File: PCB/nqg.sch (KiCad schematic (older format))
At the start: 76 parts, among them SW1 SW_PUSH, SW10 SW_PUSH, SW11 SW_PUSH, SW12 SW_PUSH, SW13 SW_PUSH, SW14 SW_PUSH, SW15 SW_PUSH, SW16 SW_PUSH, SW17 SW_PUSH, SW18 SW_PUSH, SW19 SW_PUSH, SW2 SW_PUSH, SW20 SW_PUSH, SW21 SW_PUSH, SW22 SW_PUSH, SW23 SW_PUSH, SW24 SW_PUSH, SW25 SW_PUSH, SW26 SW_PUSH, SW27 SW_PUSH, SW28 SW_PUSH, SW29 SW_PUSH, SW3 SW_PUSH, SW30 SW_PUSH, SW31 SW_PUSH, SW32 SW_PUSH, SW33 SW_PUSH, SW34 SW_PUSH, SW35 SW_PUSH, SW36 SW_PUSH, SW37 SW_PUSH, SW38 SW_PUSH, SW39 SW_PUSH, SW4 SW_PUSH, SW40 SW_PUSH, SW5 SW_PUSH, SW6 SW_PUSH, SW7 SW_PUSH, SW8 SW_PUSH, SW9 SW_PUSH, U1 ProMicro

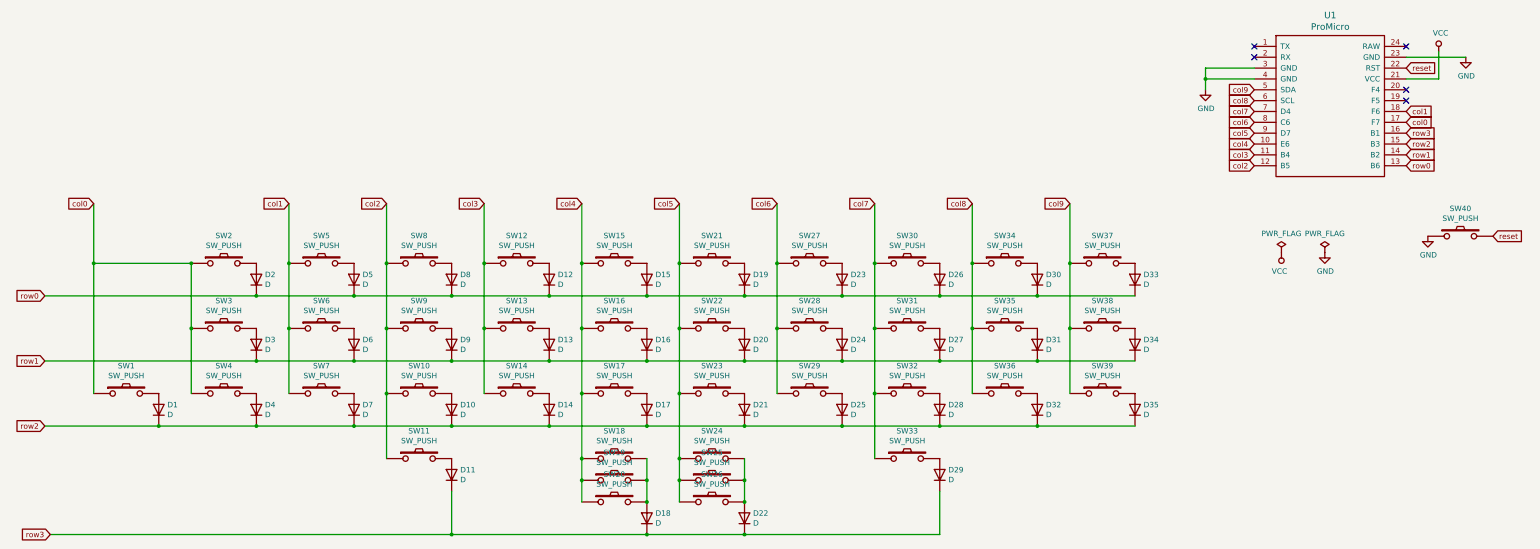
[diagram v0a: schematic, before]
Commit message: redid wiring, firmware halfway done
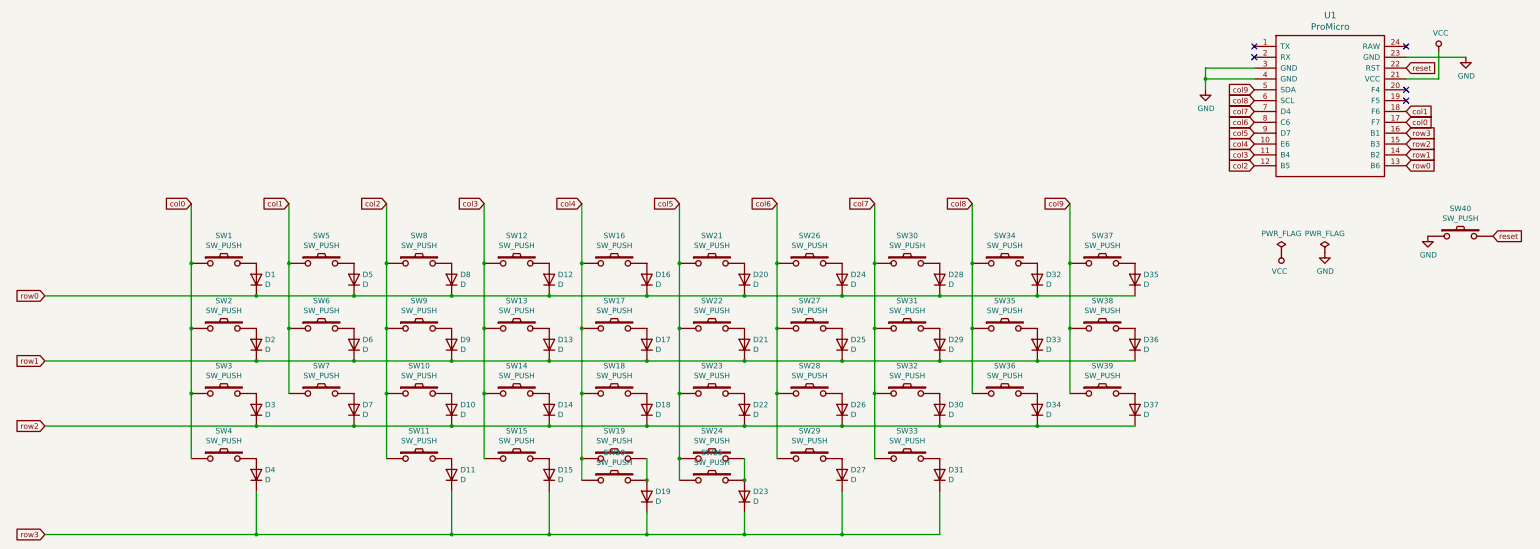
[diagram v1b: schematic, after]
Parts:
- added D15, D27: D, Diode_SMD:D_SOD-123, symbol Device:D
- renumbered D2 to D1, D15 to D16, D16 to D17, D17 to D18, D18 to D19, D3 to D2, D19 to D20, D20 to D21, D21 to D22, D22 to D23, D23 to D24, D24 to D25, D25 to D26, D26 to D28, D27 to D29, D4 to D3, D28 to D30, D29 to D31, D30 to D32, D31 to D33, D32 to D34, D33 to D35, D34 to D36, D35 to D37, D1 to D4, SW2 to SW1, SW20 to SW15, SW15 to SW16, SW16 to SW17, SW17 to SW18, SW18 to SW19, SW3 to SW2, SW19 to SW20, SW27 to SW26, SW28 to SW27, SW29 to SW28, SW26 to SW29, SW4 to SW3, SW1 to SW4
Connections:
- net col3: now also SW15.1
- net col4: no longer SW15.1
- net col5: no longer SW29.1
- net col6: now also SW29.1
- net row2: no longer D4.1 (K)
- net row3: now also D4.1 (K), D15.1 (K), D27.1 (K)
- net at D19.2 (A), SW19.2, SW20.2: no longer SW15.2
- net at D23.2 (A), SW24.2, SW25.2: no longer SW29.2
- new net: D15.2 (A), SW15.2
- new net: D27.2 (A), SW29.2
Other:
- moved on the sheet: D19, D23, D4, SW15, SW29, SW4

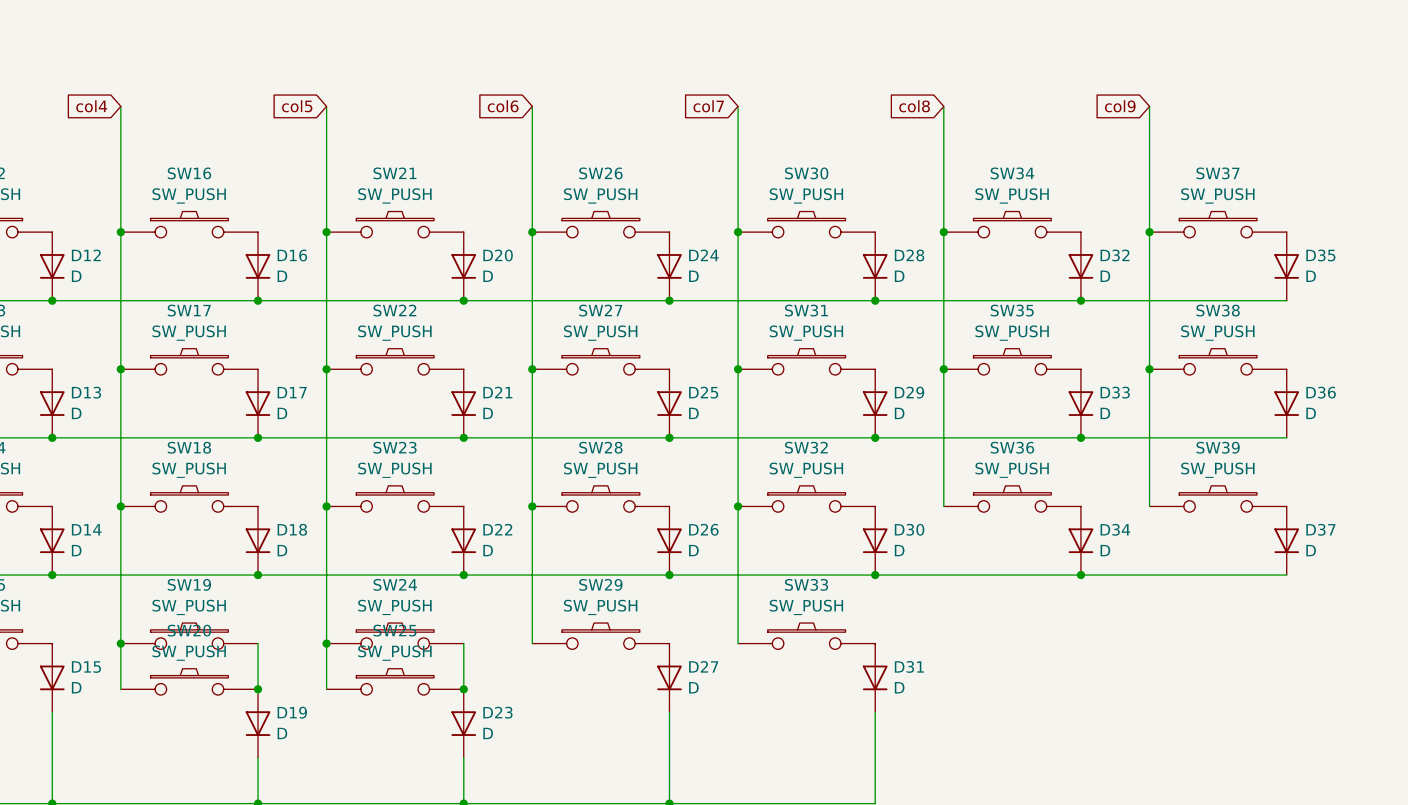
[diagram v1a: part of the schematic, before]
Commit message: now switch # matches up with diode # in SMD version as well
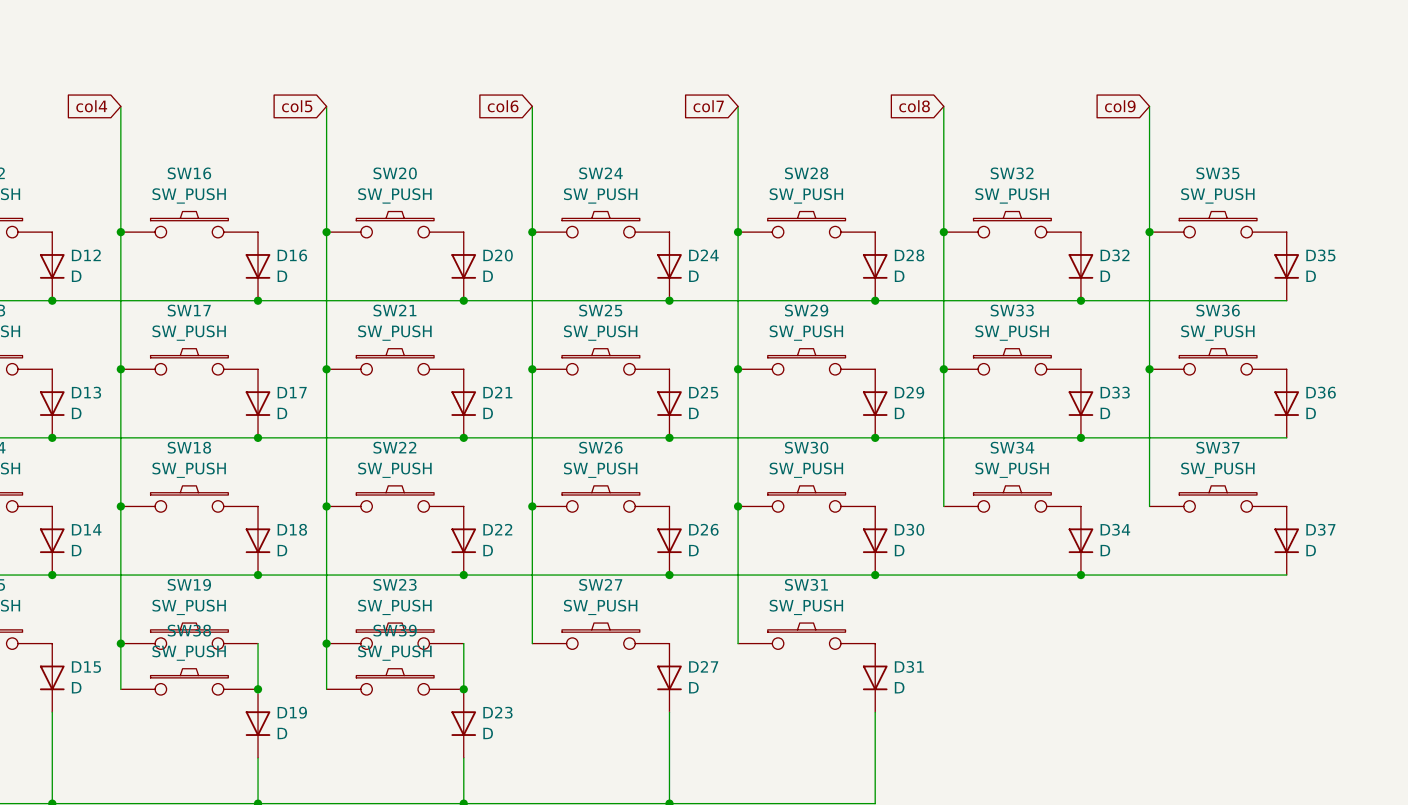
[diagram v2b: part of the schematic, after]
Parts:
- removed SW20, SW25: SW_PUSH, kbd:CherryMX_Hotswap_Back, symbol kbd:SW_PUSH
- added SW38, SW39: SW_PUSH, kbd:CherryMX_Hotswap_Back, symbol kbd:SW_PUSH
- renumbered SW21 to SW20, SW22 to SW21, SW23 to SW22, SW24 to SW23, SW26 to SW24, SW27 to SW25, SW28 to SW26, SW29 to SW27, SW30 to SW28, SW31 to SW29, SW32 to SW30, SW33 to SW31, SW34 to SW32, SW35 to SW33, SW36 to SW34, SW37 to SW35, SW38 to SW36, SW39 to SW37
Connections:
- net col4: now also SW38.1
- net col5: now also SW39.1
- net at D19.2 (A), SW19.2: now also SW38.2
- net at D23.2 (A), SW23.2: now also SW39.2
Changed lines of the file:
@@
 EESchema Schematic File Version 4
 LIBS:nqg-cache
-EELAYER 26 0
+EELAYER 29 0
 EELAYER END
 $Descr A3 16535 11693
@@
 	12350 1850 12350 1950
 $Comp
-L kbd:SW_PUSH SW40
-U 1 1 5C8B7B86
-P 14700 3300
-F 0 "SW40" H 14700 3555 50  0000 C CNN
-F 1 "SW_PUSH" H 14700 3464 50  0000 C CNN
-F 2 "kbd:ResetSW" H 14700 3300 50  0001 C CNN
-F 3 "" H 14700 3300 50  0000 C CNN
-	1    14700 3300
-	1    0    0    -1
-$EndComp
-$Comp
 L power:GND #PWR04
 U 1 1 5C8B7C12
@@
 $EndComp
 $Comp
-L kbd:SW_PUSH SW21
+L kbd:SW_PUSH SW20
 U 1 1 5C8B7DA2
 P 7800 3550
-F 0 "SW21" H 7800 3805 50  0000 C CNN
+F 0 "SW20" H 7800 3805 50  0000 C CNN
 F 1 "SW_PUSH" H 7800 3714 50  0000 C CNN
 F 2 "kbd:CherryMX_Hotswap_Back" H 7800 3550 50  0001 C CNN
@@
 $EndComp
 $Comp
-L kbd:SW_PUSH SW26
+L kbd:SW_PUSH SW24
 U 1 1 5C8B7E2C
 P 8700 3550
-F 0 "SW26" H 8700 3805 50  0000 C CNN
+F 0 "SW24" H 8700 3805 50  0000 C CNN
 F 1 "SW_PUSH" H 8700 3714 50  0000 C CNN
 F 2 "kbd:CherryMX_Hotswap_Back" H 8700 3550 50  0001 C CNN
@@
 $EndComp
 $Comp
-L kbd:SW_PUSH SW30
+L kbd:SW_PUSH SW28
 U 1 1 5C8B7E33
 P 9600 3550
-F 0 "SW30" H 9600 3805 50  0000 C CNN
+F 0 "SW28" H 9600 3805 50  0000 C CNN
 F 1 "SW_PUSH" H 9600 3714 50  0000 C CNN
 F 2 "kbd:CherryMX_Hotswap_Back" H 9600 3550 50  0001 C CNN
@@
 $EndComp
 $Comp
-L kbd:SW_PUSH SW34
+L kbd:SW_PUSH SW32
 U 1 1 5C8B7ECE
 P 10500 3550
-F 0 "SW34" H 10500 3805 50  0000 C CNN
+F 0 "SW32" H 10500 3805 50  0000 C CNN
 F 1 "SW_PUSH" H 10500 3714 50  0000 C CNN
 F 2 "kbd:CherryMX_Hotswap_Back" H 10500 3550 50  0001 C CNN
@@
 $EndComp
 $Comp
-L kbd:SW_PUSH SW37
+L kbd:SW_PUSH SW35
 U 1 1 5C8B7ED5
 P 11400 3550
-F 0 "SW37" H 11400 3805 50  0000 C CNN
+F 0 "SW35" H 11400 3805 50  0000 C CNN
 F 1 "SW_PUSH" H 11400 3714 50  0000 C CNN
 F 2 "kbd:CherryMX_Hotswap_Back" H 11400 3550 50  0001 C CNN
@@
 $EndComp
 $Comp
-L kbd:SW_PUSH SW22
+L kbd:SW_PUSH SW21
 U 1 1 5C8B8CA4
 P 7800 4150
-F 0 "SW22" H 7800 4405 50  0000 C CNN
+F 0 "SW21" H 7800 4405 50  0000 C CNN
 F 1 "SW_PUSH" H 7800 4314 50  0000 C CNN
 F 2 "kbd:CherryMX_Hotswap_Back" H 7800 4150 50  0001 C CNN
@@
 $EndComp
 $Comp
-L kbd:SW_PUSH SW27
+L kbd:SW_PUSH SW25
 U 1 1 5C8B8CAB
 P 8700 4150
-F 0 "SW27" H 8700 4405 50  0000 C CNN
+F 0 "SW25" H 8700 4405 50  0000 C CNN
 F 1 "SW_PUSH" H 8700 4314 50  0000 C CNN
 F 2 "kbd:CherryMX_Hotswap_Back" H 8700 4150 50  0001 C CNN
@@
 $EndComp
 $Comp
-L kbd:SW_PUSH SW31
+L kbd:SW_PUSH SW29
 U 1 1 5C8B8CB2
 P 9600 4150
-F 0 "SW31" H 9600 4405 50  0000 C CNN
+F 0 "SW29" H 9600 4405 50  0000 C CNN
 F 1 "SW_PUSH" H 9600 4314 50  0000 C CNN
 F 2 "kbd:CherryMX_Hotswap_Back" H 9600 4150 50  0001 C CNN
@@
 $EndComp
 $Comp
-L kbd:SW_PUSH SW35
+L kbd:SW_PUSH SW33
 U 1 1 5C8B8CB9
 P 10500 4150
-F 0 "SW35" H 10500 4405 50  0000 C CNN
+F 0 "SW33" H 10500 4405 50  0000 C CNN
 F 1 "SW_PUSH" H 10500 4314 50  0000 C CNN
 F 2 "kbd:CherryMX_Hotswap_Back" H 10500 4150 50  0001 C CNN
@@
 $EndComp
 $Comp
-L kbd:SW_PUSH SW38
+L kbd:SW_PUSH SW36
 U 1 1 5C8B8CC0
 P 11400 4150
-F 0 "SW38" H 11400 4405 50  0000 C CNN
+F 0 "SW36" H 11400 4405 50  0000 C CNN
 F 1 "SW_PUSH" H 11400 4314 50  0000 C CNN
 F 2 "kbd:CherryMX_Hotswap_Back" H 11400 4150 50  0001 C CNN
@@
 $EndComp
 $Comp
-L kbd:SW_PUSH SW23
+L kbd:SW_PUSH SW22
 U 1 1 5C8B8E1E
 P 7800 4750
-F 0 "SW23" H 7800 5005 50  0000 C CNN
+F 0 "SW22" H 7800 5005 50  0000 C CNN
 F 1 "SW_PUSH" H 7800 4914 50  0000 C CNN
 F 2 "kbd:CherryMX_Hotswap_Back" H 7800 4750 50  0001 C CNN
@@
 $EndComp
 $Comp
-L kbd:SW_PUSH SW28
+L kbd:SW_PUSH SW26
 U 1 1 5C8B8E25
 P 8700 4750
-F 0 "SW28" H 8700 5005 50  0000 C CNN
+F 0 "SW26" H 8700 5005 50  0000 C CNN
 F 1 "SW_PUSH" H 8700 4914 50  0000 C CNN
 F 2 "kbd:CherryMX_Hotswap_Back" H 8700 4750 50  0001 C CNN
@@
 $EndComp
 $Comp
-L kbd:SW_PUSH SW32
+L kbd:SW_PUSH SW30
 U 1 1 5C8B8E2C
 P 9600 4750
-F 0 "SW32" H 9600 5005 50  0000 C CNN
+F 0 "SW30" H 9600 5005 50  0000 C CNN
 F 1 "SW_PUSH" H 9600 4914 50  0000 C CNN
 F 2 "kbd:CherryMX_Hotswap_Back" H 9600 4750 50  0001 C CNN
@@
 $EndComp
 $Comp
-L kbd:SW_PUSH SW36
+L kbd:SW_PUSH SW34
 U 1 1 5C8B8E33
 P 10500 4750
-F 0 "SW36" H 10500 5005 50  0000 C CNN
+F 0 "SW34" H 10500 5005 50  0000 C CNN
 F 1 "SW_PUSH" H 10500 4914 50  0000 C CNN
 F 2 "kbd:CherryMX_Hotswap_Back" H 10500 4750 50  0001 C CNN
@@
 $EndComp
 $Comp
-L kbd:SW_PUSH SW39
+L kbd:SW_PUSH SW37
 U 1 1 5C8B8E3A
 P 11400 4750
-F 0 "SW39" H 11400 5005 50  0000 C CNN
+F 0 "SW37" H 11400 5005 50  0000 C CNN
 F 1 "SW_PUSH" H 11400 4914 50  0000 C CNN
 F 2 "kbd:CherryMX_Hotswap_Back" H 11400 4750 50  0001 C CNN
@@
 $EndComp
 $Comp
-L kbd:SW_PUSH SW24
+L kbd:SW_PUSH SW23
 U 1 1 5C8B96FC
 P 7800 5350
-F 0 "SW24" H 7800 5605 50  0000 C CNN
+F 0 "SW23" H 7800 5605 50  0000 C CNN
 F 1 "SW_PUSH" H 7800 5514 50  0000 C CNN
 F 2 "kbd:CherryMX_Hotswap_Back" H 7800 5350 50  0001 C CNN
@@
 $EndComp
 $Comp
-L kbd:SW_PUSH SW33
+L kbd:SW_PUSH SW31
 U 1 1 5C8B97A7
 P 9600 5350
-F 0 "SW33" H 9600 5605 50  0000 C CNN
+F 0 "SW31" H 9600 5605 50  0000 C CNN
 F 1 "SW_PUSH" H 9600 5514 50  0000 C CNN
 F 2 "kbd:CherryMX_Hotswap_Back" H 9600 5350 50  0001 C CNN
@@
 NoConn ~ 12800 1550
 $Comp
-L kbd:SW_PUSH SW20
-U 1 1 5C8F7CB2
-P 6900 5550
-F 0 "SW20" H 6900 5805 50  0000 C CNN
-F 1 "SW_PUSH" H 6900 5714 50  0000 C CNN
-F 2 "kbd:CherryMX_Hotswap_Back" H 6900 5550 50  0001 C CNN
-F 3 "" H 6900 5550 50  0000 C CNN
-	1    6900 5550
-	1    0    0    -1
-$EndComp
-$Comp
 L kbd:SW_PUSH SW15
 U 1 1 5C8F7DE0
@@
 $EndComp
 $Comp
-L kbd:SW_PUSH SW25
-U 1 1 5C8F7F08
-P 7800 5550
-F 0 "SW25" H 7800 5805 50  0000 C CNN
-F 1 "SW_PUSH" H 7800 5714 50  0000 C CNN
-F 2 "kbd:CherryMX_Hotswap_Back" H 7800 5550 50  0001 C CNN
-F 3 "" H 7800 5550 50  0000 C CNN
-	1    7800 5550
-	1    0    0    -1
-$EndComp
-$Comp
-L kbd:SW_PUSH SW29
+L kbd:SW_PUSH SW27
 U 1 1 5C8F811E
 P 8700 5350
-F 0 "SW29" H 8700 5605 50  0000 C CNN
+F 0 "SW27" H 8700 5605 50  0000 C CNN
 F 1 "SW_PUSH" H 8700 5514 50  0000 C CNN
 F 2 "kbd:CherryMX_Hotswap_Back" H 8700 5350 50  0001 C CNN
@@
 	8400 4750 8400 5350
 Connection ~ 8400 4750
-Connection ~ 8100 5550
-Connection ~ 7200 5550
 Wire Wire Line
 	7200 5850 7200 6050
@@
 Wire Wire Line
 	8100 6050 9000 6050
+$Comp
+L kbd:SW_PUSH SW38
+U 1 1 5CBCB3A7
+P 6900 5550
+F 0 "SW38" H 6900 5805 50  0000 C CNN
+F 1 "SW_PUSH" H 6900 5714 50  0000 C CNN
+F 2 "kbd:CherryMX_Hotswap_Back" H 6900 5550 50  0001 C CNN
+F 3 "" H 6900 5550 50  0000 C CNN
+	1    6900 5550
+	1    0    0    -1
+$EndComp
+Connection ~ 7200 5550
+$Comp
+L kbd:SW_PUSH SW39
+U 1 1 5CBCB61A
+P 7800 5550
+F 0 "SW39" H 7800 5805 50  0000 C CNN
+F 1 "SW_PUSH" H 7800 5714 50  0000 C CNN
+F 2 "kbd:CherryMX_Hotswap_Back" H 7800 5550 50  0001 C CNN
+F 3 "" H 7800 5550 50  0000 C CNN
+	1    7800 5550
+	1    0    0    -1
+$EndComp
+Connection ~ 8100 5550
+$Comp
+L kbd:SW_PUSH SW40
+U 1 1 5CBCB9A1
+P 14700 3300
+F 0 "SW40" H 14700 3555 50  0000 C CNN
+F 1 "SW_PUSH" H 14700 3464 50  0000 C CNN
+F 2 "kbd:ResetSW" H 14700 3300 50  0001 C CNN
+F 3 "" H 14700 3300 50  0000 C CNN
+	1    14700 3300
+	1    0    0    -1
+$EndComp
 $EndSCHEMATC
